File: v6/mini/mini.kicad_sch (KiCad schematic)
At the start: 0 parts

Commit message: Redesign of ENV6.mini
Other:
- company: (none) -> UDE-IES
- title: (none) -> elasticAI.hardware (ENV6.mini)
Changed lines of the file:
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@@
 	(generator_version "10.0")
 	(paper "A4")
+	(title_block
+		(title "elasticAI.hardware (ENV6.mini)")
+		(date "2026-07-03")
+		(rev "1v1")
+		(company "UDE-IES")
+	)
 	(sheet
 		(at 40.64 45.72)

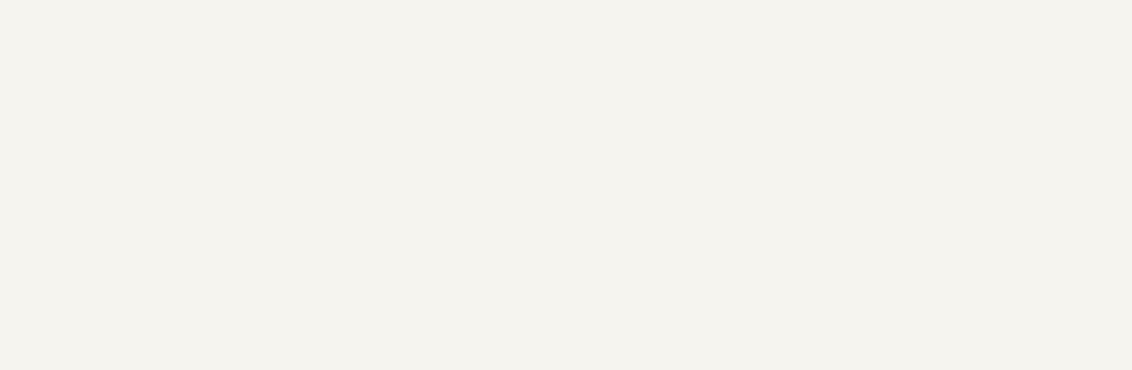
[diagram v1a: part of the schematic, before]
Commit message: Add fourth PAC sensor to ENV6mini
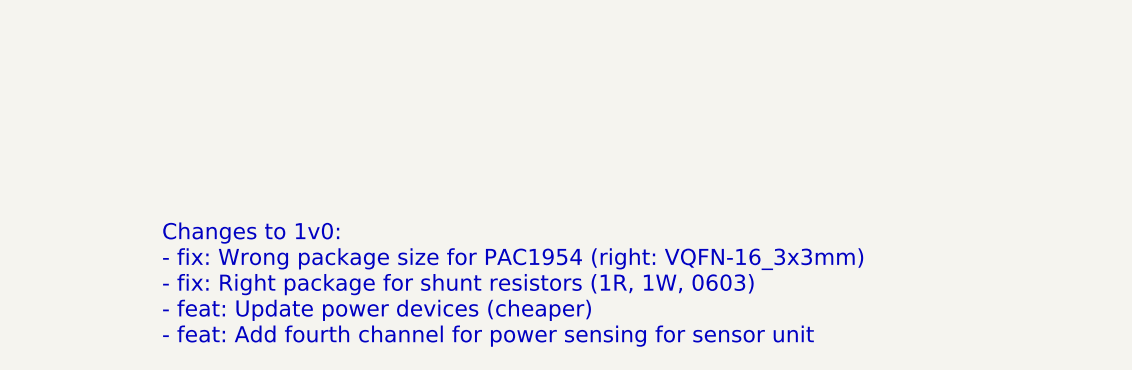
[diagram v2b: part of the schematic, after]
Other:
- note added: "Changes to 1v0: - fix: Wrong package size for PAC1954 (right: VQFN-16_3x3mm) - fix: Right package for shunt resistors (1R, 1W, 0603) - feat: Update power devices (cheaper) - feat: Add fourth channel for power sensing for sensor unit"
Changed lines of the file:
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@@
 		(company "UDE-IES")
+	)
+	(text "Changes to 1v0:\n- fix: Wrong package size for PAC1954 (right: VQFN-16_3x3mm)\n- fix: Right package for shunt resistors (1R, 1W, 0603)\n- feat: Update power devices (cheaper)\n- feat: Add fourth channel for power sensing for sensor unit"
+		(exclude_from_sim no)
+		(at 177.546 165.1 0)
+		(effects
+			(font
+				(size 1.778 1.778)
+			)
+			(justify left bottom)
+		)
 	)
 	(sheet

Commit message: Fixed errors in ENV6mini
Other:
- note added: "Changes to 1v0: - fix: Wrong package size for PAC1954 (right: VQFN-16_3x3mm) - fix: Right package for shunt resistors (1R, 1W, 0603) - feat: Update power devices (cheaper) - feat: Add fourth channel for power sensing for sensor unit - fix: Remove I2C from FPGA - Add fiducials for automatic assembling"
- note removed: "Changes to 1v0: - fix: Wrong package size for PAC1954 (right: VQFN-16_3x3mm) - fix: Right package for shunt resistors (1R, 1W, 0603) - feat: Update power devices (cheaper) - feat: Add fourth channel for power sensing for sensor unit"
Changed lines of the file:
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@@
 		(company "UDE-IES")
 	)
-	(text "Changes to 1v0:\n- fix: Wrong package size for PAC1954 (right: VQFN-16_3x3mm)\n- fix: Right package for shunt resistors (1R, 1W, 0603)\n- feat: Update power devices (cheaper)\n- feat: Add fourth channel for power sensing for sensor unit"
+	(text "Changes to 1v0:\n- fix: Wrong package size for PAC1954 (right: VQFN-16_3x3mm)\n- fix: Right package for shunt resistors (1R, 1W, 0603)\n- feat: Update power devices (cheaper)\n- feat: Add fourth channel for power sensing for sensor unit\n- fix: Remove I2C from FPGA\n- Add fiducials for automatic assembling"
 		(exclude_from_sim no)
 		(at 177.546 165.1 0)
